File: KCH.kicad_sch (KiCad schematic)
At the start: 0 parts

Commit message: Initial schematic
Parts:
- added C?: (no value), symbol Device:C
- added D?: (no value), symbol Device:D_TVS
- added H1, H2, H3, H4: (no value), symbol Mechanical:MountingHole
- added J3: (no value), symbol KCH:OX40HAT
- added J?: (no value), symbol Connector_Generic:Conn_01x02
- added JP?: (no value), symbol Jumper:SolderJumper_2_Open
- added R? (x3): (no value), symbol Device:R
- added U?: (no value), symbol KCH:CAT24C32WI
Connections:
- new net: JP?.1 (A), R?.2, U?.7 (WP)
- new net GND: C?.2, J3.14 (GND), J3.20 (GND), J3.25 (GND), J3.30 (GND), J3.34 (GND), J3.39 (GND), J3.6 (GND), J3.9 (GND), JP?.2 (B), U?.1 (A0), U?.2 (A1), U?.3 (A2), U?.4 (GND)
- new net GPIO10: J3.19 (BCM10)
- new net GPIO11: J3.23 (BCM11)
- new net GPIO12: J3.32 (BCM12)
- new net GPIO13: J3.33 (BCM13)
- new net GPIO16: J3.36 (BCM16)
- new net GPIO17: J3.11 (BCM17)
- new net GPIO18: J3.12 (BCM18)
- new net GPIO19: J3.35 (BCM19)
- new net GPIO20: J3.38 (BCM20)
- new net GPIO21: J3.40 (BCM21)
- new net GPIO22: J3.15 (BCM22)
- new net GPIO23: J3.16 (BCM23)
- new net GPIO24: J3.18 (BCM24)
- new net GPIO25: J3.22 (BCM25)
- new net GPIO26: J3.37 (BCM26)
- new net GPIO27: J3.13 (BCM27)
- new net GPIO4: J3.7 (BCM4)
- new net GPIO5: J3.29 (BCM5)
- new net GPIO6: J3.31 (BCM6)
- new net GPIO7: J3.26 (BCM7)
- new net GPIO8: J3.24 (BCM8)
- new net GPIO9: J3.21 (BCM9)
- new net ID_SC_EEPROM: J3.28 (BCM1), R?.2, U?.6 (SCL)
- new net ID_SD_EEPROM: J3.27 (BCM0), R?.2, U?.5 (SDA)
- new net P3V3_HAT: C?.1, J3.1 (P3V3), J3.17 (P3V3), R?.1, R?.1, R?.1, U?.8 (VCC)
- new net P5V_HAT: J3.2 (P5V), J3.4 (P5V)
- new net Power/12V: D?.1 (A1), J?.1 (Pin_1)
- new net Power/PGND: D?.2 (A2), J?.2 (Pin_2)
- new net SCL: J3.5 (BCM3)
- new net SDA: J3.3 (BCM2)
- new net UART_RXD: J3.10 (BCM15)
- new net UART_TXD: J3.8 (BCM14)
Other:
- added sheet LED UI (led.kicad_sch)
- added sheet Power (power.kicad_sch)
- added sheet RGB LED UI (rgb_led.kicad_sch)
- note added: "40-Pin HAT Connector"
- note added: "GPIO8 is used for boot 20% so SPI CS function can be used to drive the pin from the device tree"
- note added: "GPIOs for each LED can be swapped during layout PWM available on GPIO12/13"
- note added: "HAT EEPROM"
- note added: "Mounting Holes"
- title: (none) -> Raspberry Pi HAT

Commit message: More refinement
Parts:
- removed JP?: (no value), symbol Jumper:SolderJumper_2_Open
- added C1: (no value), symbol Device:C
- added J2: (no value), symbol Connector:TestPoint_2Pole
- gave numbers to parts that had none: 7
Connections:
- net GND: now also J2.1
- net P3V3_HAT: no longer J3.1 (P3V3)
- net Power/12V: now also C1.2
- net Power/PGND: now also C1.1
- net at R1.2, U1.7 (WP): now also J2.2
- net P5V_HAT renamed +5V
- no-connect marks 0 -> 1
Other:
- sheet LED UI ports: added none; removed 5V
- sheet RGB LED UI ports: added none; removed 5V
- note added: "12V In"
- note added: "GPIOs for each LED can be swapped during layout Except GPIO7 is used for boot 20% so SPI CS function can be used to drive the pin from the device tree. PWM available on GPIO12/13"
- note added: "Mounting holes according to Raspberry Pi hat spec"
- note removed: "GPIO8 is used for boot 20% so SPI CS function can be used to drive the pin from the device tree"
- note removed: "GPIOs for each LED can be swapped during layout PWM available on GPIO12/13"
- company: (none) -> Student Robotics
- moved on the sheet: C2, D1, H1, H2, H3, H4, J3, R1, R2, R3, U1

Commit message: Schematic revision S1
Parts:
- D1: value (none) -> D_TVS
- H1, H2, H3, H4: value (none) -> 3mm_Mounting_Hole; footprint (none) -> project_footprints:NPTH_3mm_ID
- J1: value (none) -> CTBP9550/2
- J2: value (none) -> Write EEPROM; footprint (none) -> Connector_PinHeader_2.54mm:PinHeader_1x02_P2.54mm_Vertical
- J3: value (none) -> 40HAT; footprint (none) -> Connector_PinSocket_2.54mm:PinSocket_2x20_P2.54mm_Vertical
- R1, R2, R3: footprint (none) -> Resistor_SMD:R_0603_1608Metric_Pad0.84x1.00mm_HandSolder
- U1: value (none) -> CAT24C32WI; footprint (none) -> Package_SO:SOIC-8_3.9x4.9mm_P1.27mm
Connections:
- net P3V3_HAT renamed +3V3
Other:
- moved on the sheet: C1

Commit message: Pre-review improvements
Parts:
- added J4: Serial, Connector_PinHeader_2.54mm:PinHeader_1x06_P2.54mm_Vertical, symbol Connector:Conn_01x06_Male
- C1, C2: value (none) -> 100n; footprint (none) -> Capacitor_SMD:C_0402_1005Metric
- D1: value D_TVS -> SMAJ15CA; footprint (none) -> Diode_SMD:D_SMA
- H1, H2, H3, H4, J2: now left out of the parts list
- R1: value (none) -> 1k; footprint Resistor_SMD:R_0603_1608Metric_Pad0.84x1.00mm_HandSolder -> Resistor_SMD:R_0402_1005Metric
- R2, R3: value (none) -> 3k9; footprint Resistor_SMD:R_0603_1608Metric_Pad0.84x1.00mm_HandSolder -> Resistor_SMD:R_0402_1005Metric
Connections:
- net GND: now also J4.1 (Pin_1)
- net UART_RXD: now also J4.4 (Pin_4)
- net UART_TXD: now also J4.5 (Pin_5)
- no-connect marks 1 -> 4
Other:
- note added: "Serial Interface"

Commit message: Add remaining footprints
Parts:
- J1: footprint (none) -> project_footprints:CTBP9550-2
- J4: now left out of the parts list
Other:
- note added: "Not populated as standard"
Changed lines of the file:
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@@
     (effects (font (size 1.27 1.27)) (justify left bottom))
   )
-  (text "Serial Interface" (at 132.08 106.045 0)
+  (text "Serial Interface" (at 135.89 111.125 0)
     (effects (font (size 2.9972 2.9972) (thickness 0.5994) bold) (justify left bottom))
   )
   (text "HAT EEPROM" (at 206.375 27.305 0)
     (effects (font (size 3 3) (thickness 0.6) bold) (justify left bottom))
+  )
+  (text "Not populated as standard" (at 141.605 131.445 0)
+    (effects (font (size 1.27 1.27)) (justify left bottom))
   )
   (label "ID_SD_EEPROM" (at 34.29 120.65 0)
@@
     (property "Reference" "J1" (id 0) (at 29.845 30.48 0))
     (property "Value" "CTBP9550/2" (id 1) (at 29.845 33.02 0))
-    (property "Footprint" "" (id 2) (at 29.845 36.83 0)
+    (property "Footprint" "project_footprints:CTBP9550-2" (id 2) (at 29.845 36.83 0)
       (effects (font (size 1.27 1.27)) hide)
     )
@@
   )
   (symbol (lib_id "Connector:Conn_01x06_Male") (at 161.925 118.745 0) (mirror y) (unit 1)
-    (in_bom yes) (on_board yes) (fields_autoplaced)
-    (property "Reference" "J4" (id 0) (at 161.29 107.95 0))
-    (property "Value" "Serial" (id 1) (at 161.29 110.49 0))
+    (in_bom no) (on_board yes) (fields_autoplaced)
+    (property "Reference" "J4" (id 0) (at 163.83 118.7449 0)
+      (effects (font (size 1.27 1.27)) (justify right))
+    )
+    (property "Value" "Serial" (id 1) (at 163.83 121.2849 0)
+      (effects (font (size 1.27 1.27)) (justify right))
+    )
     (property "Footprint" "Connector_PinHeader_2.54mm:PinHeader_1x06_P2.54mm_Vertical" (id 2) (at 161.925 118.745 0)
       (effects (font (size 1.27 1.27)) hide)
@@
     )
     (path "/b4b3b701-a899-490d-ae85-bed6fac6ac68/914985c9-f53c-4071-8ac7-72deb7281b12"
-      (reference "D17") (unit 1) (value "FM-B2020RGBA-HG") (footprint "")
+      (reference "D17") (unit 1) (value "FM-B2020RGBA-HG") (footprint "project_footprints:FM-B2020RGBA-HG")
     )
     (path "/b4b3b701-a899-490d-ae85-bed6fac6ac68/6794becf-4cea-44b0-91d3-a7f1be26802d"
-      (reference "D18") (unit 1) (value "FM-B2020RGBA-HG") (footprint "")
+      (reference "D18") (unit 1) (value "FM-B2020RGBA-HG") (footprint "project_footprints:FM-B2020RGBA-HG")
     )
     (path "/b4b3b701-a899-490d-ae85-bed6fac6ac68/206519a6-2a7f-4f8e-a79d-f8e00231e9d2"
-      (reference "D19") (unit 1) (value "FM-B2020RGBA-HG") (footprint "")
+      (reference "D19") (unit 1) (value "FM-B2020RGBA-HG") (footprint "project_footprints:FM-B2020RGBA-HG")
     )
     (path "/b4b3b701-a899-490d-ae85-bed6fac6ac68/661f2887-316f-4c60-94a5-48a6f8725a92"
-      (reference "D20") (unit 1) (value "FM-B2020RGBA-HG") (footprint "")
+      (reference "D20") (unit 1) (value "FM-B2020RGBA-HG") (footprint "project_footprints:FM-B2020RGBA-HG")
     )
     (path "/b972d901-8d26-4685-bdf5-467543b91602/b6f313c7-2466-491b-91f3-2cb16f51eb47"
@@
     )
     (path "/4b63b8f6-4ecc-4e17-ba18-3581427d8196"
-      (reference "J1") (unit 1) (value "CTBP9550/2") (footprint "")
+      (reference "J1") (unit 1) (value "CTBP9550/2") (footprint "project_footprints:CTBP9550-2")
     )
     (path "/05b42443-4e19-4534-a6d5-3fd419f2f9c9"
@@
     )
     (path "/b972d901-8d26-4685-bdf5-467543b91602/7beb067c-0b7f-4f24-a971-20f7e9559c78"
-      (reference "L1") (unit 1) (value "10uH") (footprint "")
+      (reference "L1") (unit 1) (value "10uH") (footprint "project_footprints:MWSA0603")
     )
     (path "/b972d901-8d26-4685-bdf5-467543b91602/8e325b52-0146-4b64-b3bb-5217b6f59bd9"

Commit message: Updates for version S2
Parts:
- H1, H2, H3, H4: footprint project_footprints:NPTH_3mm_ID -> MountingHole:MountingHole_3.2mm_M3_ISO14580_Pad; symbol Mechanical:MountingHole -> Mechanical:MountingHole_Pad
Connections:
- net GND: now also H1.1, H2.1, H3.1, H4.1
- net SCL: no longer names the net of J3.5 (BCM3)
- net SDA: no longer names the net of J3.3 (BCM2)
- no-connect marks 4 -> 6
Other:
- title: Raspberry Pi HAT -> KCH - Raspberry Pi HAT

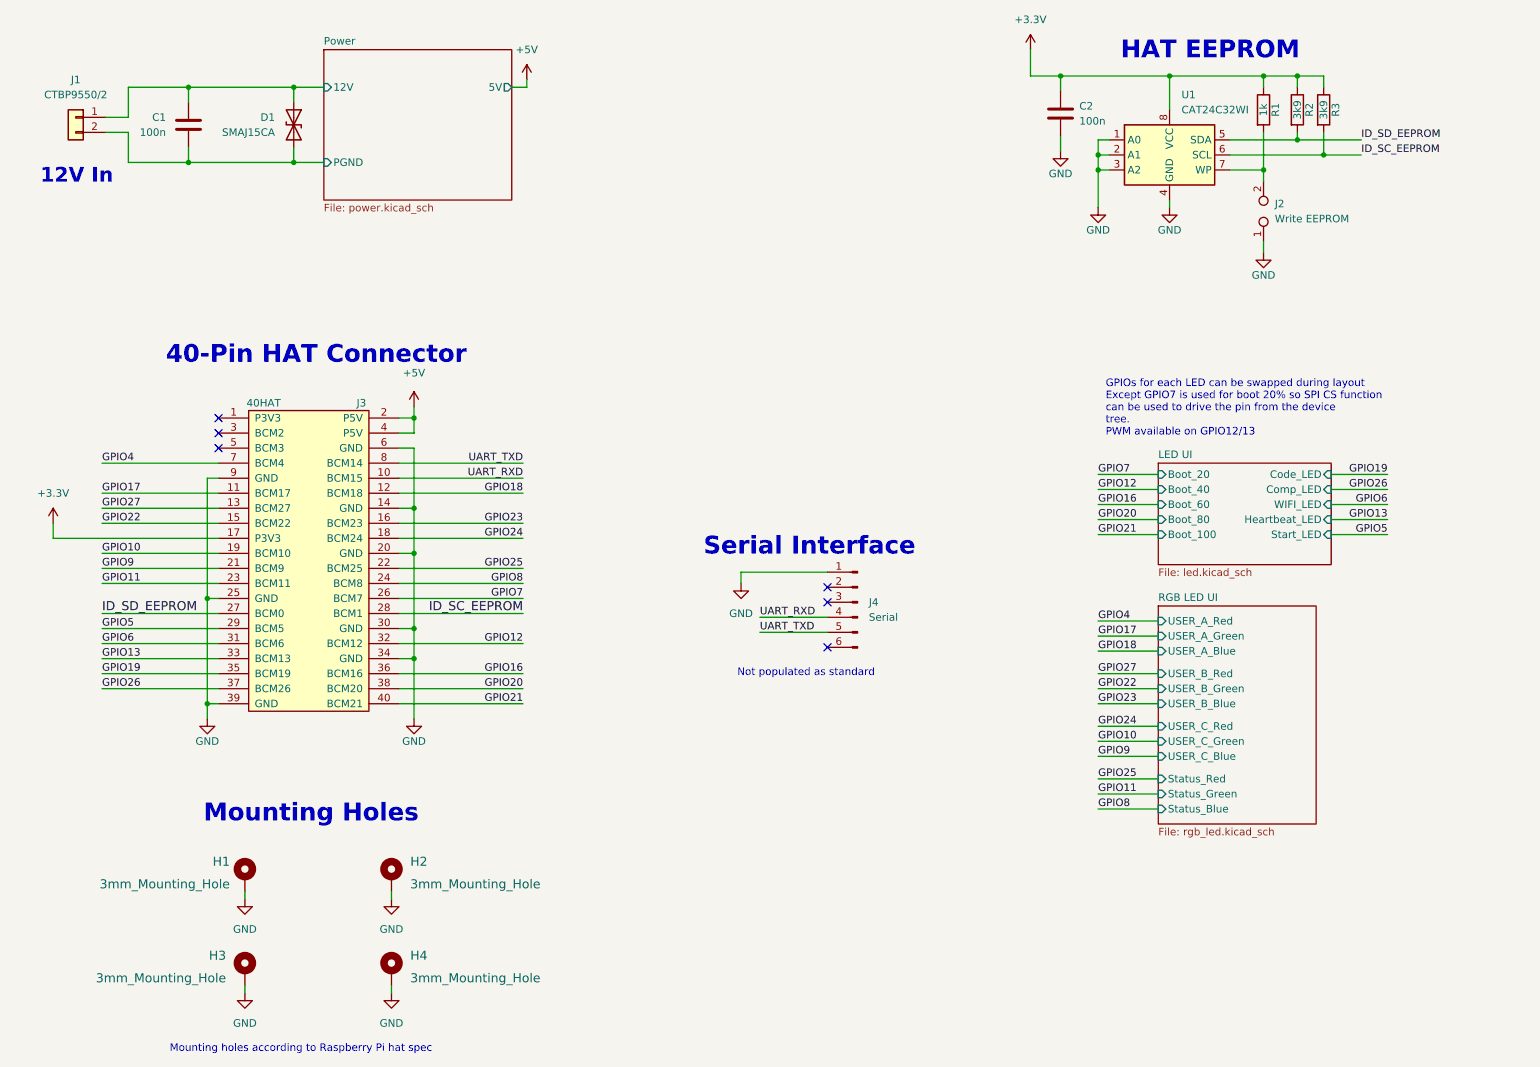
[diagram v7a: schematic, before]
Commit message: V1 of the layout
In line with spec.md and subject to review.
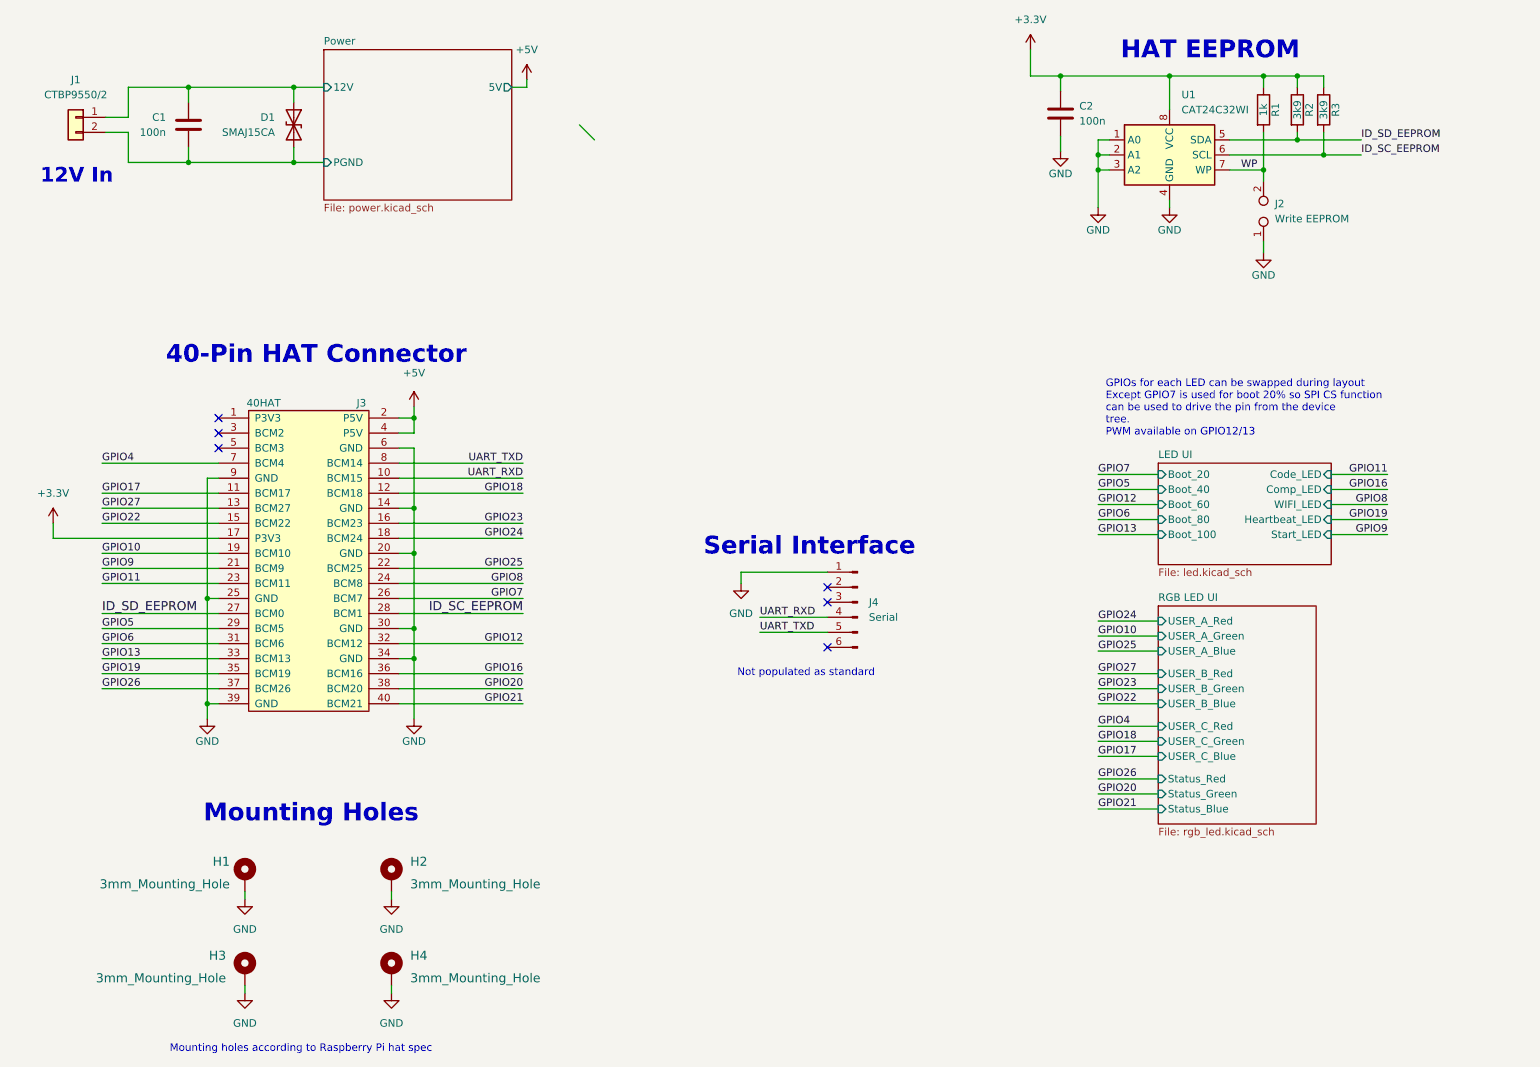
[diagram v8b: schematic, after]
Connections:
- net WP: now reaches J2.2, R1.2, U1.7 (WP)
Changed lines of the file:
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@@
   (no_connect (at 53.975 90.17))
   (no_connect (at 53.975 87.63))
+  (bus_entry (at 114.935 38.1) (size 2.54 2.54)
+    (stroke (width 0) (type default) (color 0 0 0 0))
+  )
   (wire (pts (xy 84.455 113.03) (xy 105.41 113.03))
     (stroke (width 0) (type default) (color 0 0 0 0))
@@
     (effects (font (size 1.524 1.524)) (justify left bottom))
   )
-  (label "GPIO27" (at 202.565 130.81 0)
-    (effects (font (size 1.27 1.27)) (justify left bottom))
-  )
-  (label "GPIO4" (at 202.565 121.92 0)
-    (effects (font (size 1.27 1.27)) (justify left bottom))
-  )
-  (label "GPIO12" (at 202.565 99.695 0)
-    (effects (font (size 1.27 1.27)) (justify left bottom))
-  )
-  (label "GPIO13" (at 251.46 104.775 180)
-    (effects (font (size 1.27 1.27)) (justify right bottom))
+  (label "GPIO23" (at 202.565 133.35 0)
+    (effects (font (size 1.27 1.27)) (justify left bottom))
+  )
+  (label "GPIO12" (at 202.565 102.235 0)
+    (effects (font (size 1.27 1.27)) (justify left bottom))
+  )
+  (label "GPIO26" (at 202.565 148.59 0)
+    (effects (font (size 1.27 1.27)) (justify left bottom))
   )
   (label "GPIO22" (at 34.29 105.41 0)
     (effects (font (size 1.27 1.27)) (justify left bottom))
   )
-  (label "GPIO17" (at 202.565 124.46 0)
-    (effects (font (size 1.27 1.27)) (justify left bottom))
-  )
   (label "GPIO20" (at 105.41 133.35 180)
     (effects (font (size 1.27 1.27)) (justify right bottom))
@@
     (effects (font (size 1.27 1.27)) (justify left bottom))
   )
-  (label "GPIO25" (at 202.565 148.59 0)
+  (label "GPIO5" (at 202.565 99.695 0)
+    (effects (font (size 1.27 1.27)) (justify left bottom))
+  )
+  (label "GPIO17" (at 202.565 144.78 0)
     (effects (font (size 1.27 1.27)) (justify left bottom))
   )
@@
     (effects (font (size 1.27 1.27)) (justify left bottom))
   )
-  (label "GPIO9" (at 202.565 144.78 0)
-    (effects (font (size 1.27 1.27)) (justify left bottom))
-  )
-  (label "GPIO11" (at 202.565 151.13 0)
-    (effects (font (size 1.27 1.27)) (justify left bottom))
-  )
-  (label "GPIO26" (at 251.46 99.695 180)
-    (effects (font (size 1.27 1.27)) (justify right bottom))
-  )
-  (label "GPIO8" (at 202.565 153.67 0)
+  (label "GPIO21" (at 202.565 153.67 0)
+    (effects (font (size 1.27 1.27)) (justify left bottom))
+  )
+  (label "GPIO10" (at 202.565 124.46 0)
+    (effects (font (size 1.27 1.27)) (justify left bottom))
+  )
+  (label "GPIO24" (at 202.565 121.92 0)
+    (effects (font (size 1.27 1.27)) (justify left bottom))
+  )
+  (label "GPIO13" (at 202.565 107.315 0)
     (effects (font (size 1.27 1.27)) (justify left bottom))
   )
@@
     (effects (font (size 1.27 1.27)) (justify right bottom))
   )
+  (label "GPIO7" (at 202.565 97.155 0)
+    (effects (font (size 1.27 1.27)) (justify left bottom))
+  )
   (label "UART_RXD" (at 145.415 121.285 0)
     (effects (font (size 1.27 1.27)) (justify left bottom))
@@
     (effects (font (size 1.27 1.27)) (justify right bottom))
   )
-  (label "GPIO6" (at 251.46 102.235 180)
-    (effects (font (size 1.27 1.27)) (justify right bottom))
-  )
   (label "GPIO21" (at 105.41 135.89 180)
     (effects (font (size 1.27 1.27)) (justify right bottom))
-  )
-  (label "GPIO22" (at 202.565 133.35 0)
-    (effects (font (size 1.27 1.27)) (justify left bottom))
   )
   (label "GPIO16" (at 105.41 130.81 180)
@@
     (effects (font (size 1.524 1.524)) (justify right bottom))
   )
-  (label "GPIO7" (at 202.565 97.155 0)
-    (effects (font (size 1.27 1.27)) (justify left bottom))
+  (label "GPIO16" (at 251.46 99.695 180)
+    (effects (font (size 1.27 1.27)) (justify right bottom))
   )
   (label "GPIO26" (at 34.29 133.35 0)
     (effects (font (size 1.27 1.27)) (justify left bottom))
   )
-  (label "GPIO20" (at 202.565 104.775 0)
-    (effects (font (size 1.27 1.27)) (justify left bottom))
-  )
-  (label "GPIO5" (at 251.46 107.315 180)
+  (label "GPIO19" (at 251.46 104.775 180)
+    (effects (font (size 1.27 1.27)) (justify right bottom))
+  )
+  (label "GPIO11" (at 251.46 97.155 180)
     (effects (font (size 1.27 1.27)) (justify right bottom))
   )
@@
     (effects (font (size 1.27 1.27)) (justify left bottom))
   )
+  (label "WP" (at 226.695 45.72 0)
+    (effects (font (size 1.27 1.27)) (justify left bottom))
+  )
   (label "GPIO24" (at 105.41 107.95 180)
     (effects (font (size 1.27 1.27)) (justify right bottom))
@@
     (effects (font (size 1.27 1.27)) (justify left bottom))
   )
-  (label "GPIO24" (at 202.565 139.7 0)
-    (effects (font (size 1.27 1.27)) (justify left bottom))
-  )
-  (label "GPIO21" (at 202.565 107.315 0)
-    (effects (font (size 1.27 1.27)) (justify left bottom))
-  )
   (label "UART_TXD" (at 145.415 123.825 0)
     (effects (font (size 1.27 1.27)) (justify left bottom))
   )
-  (label "GPIO23" (at 202.565 135.89 0)
-    (effects (font (size 1.27 1.27)) (justify left bottom))
-  )
   (label "GPIO8" (at 105.41 115.57 180)
     (effects (font (size 1.27 1.27)) (justify right bottom))
   )
+  (label "GPIO25" (at 202.565 127 0)
+    (effects (font (size 1.27 1.27)) (justify left bottom))
+  )
+  (label "GPIO6" (at 202.565 104.775 0)
+    (effects (font (size 1.27 1.27)) (justify left bottom))
+  )
   (label "GPIO6" (at 34.29 125.73 0)
     (effects (font (size 1.27 1.27)) (justify left bottom))
   )
-  (label "GPIO16" (at 202.565 102.235 0)
+  (label "GPIO9" (at 251.46 107.315 180)
+    (effects (font (size 1.27 1.27)) (justify right bottom))
+  )
+  (label "GPIO22" (at 202.565 135.89 0)
     (effects (font (size 1.27 1.27)) (justify left bottom))
   )
@@
     (effects (font (size 1.27 1.27)) (justify left bottom))
   )
-  (label "GPIO10" (at 202.565 142.24 0)
+  (label "GPIO18" (at 202.565 142.24 0)
+    (effects (font (size 1.27 1.27)) (justify left bottom))
+  )
+  (label "GPIO27" (at 202.565 130.81 0)
+    (effects (font (size 1.27 1.27)) (justify left bottom))
+  )
+  (label "GPIO20" (at 202.565 151.13 0)
     (effects (font (size 1.27 1.27)) (justify left bottom))
   )
@@
     (effects (font (size 1.27 1.27)) (justify right bottom))
   )
-  (label "GPIO18" (at 202.565 127 0)
-    (effects (font (size 1.27 1.27)) (justify left bottom))
+  (label "GPIO4" (at 202.565 139.7 0)
+    (effects (font (size 1.27 1.27)) (justify left bottom))
+  )
+  (label "GPIO8" (at 251.46 102.235 180)
+    (effects (font (size 1.27 1.27)) (justify right bottom))
   )
   (label "GPIO11" (at 34.29 115.57 0)
     (effects (font (size 1.27 1.27)) (justify left bottom))
-  )
-  (label "GPIO19" (at 251.46 97.155 180)
-    (effects (font (size 1.27 1.27)) (justify right bottom))
   )
   (symbol (lib_id "Mechanical:MountingHole_Pad") (at 58.42 165.1 0) (unit 1)
@@
   )
   (symbol_instances
+    (path "/b972d901-8d26-4685-bdf5-467543b91602/4f047cbf-cc74-4b99-accf-c1b41a9f89f9"
+      (reference "#FLG0101") (unit 1) (value "PWR_FLAG") (footprint "")
+    )
     (path "/ad68500b-90aa-4835-8c31-da3b08d9dadc"
       (reference "#PWR01") (unit 1) (value "GND") (footprint "")
